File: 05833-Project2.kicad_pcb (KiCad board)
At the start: 2 copper layers, 13 parts, among them J1 BB, J2 FTDI, J3 AREF, J4 GPIO, U1 LM7805, U2 ATmega328-P, Y1 16MHz Resonator

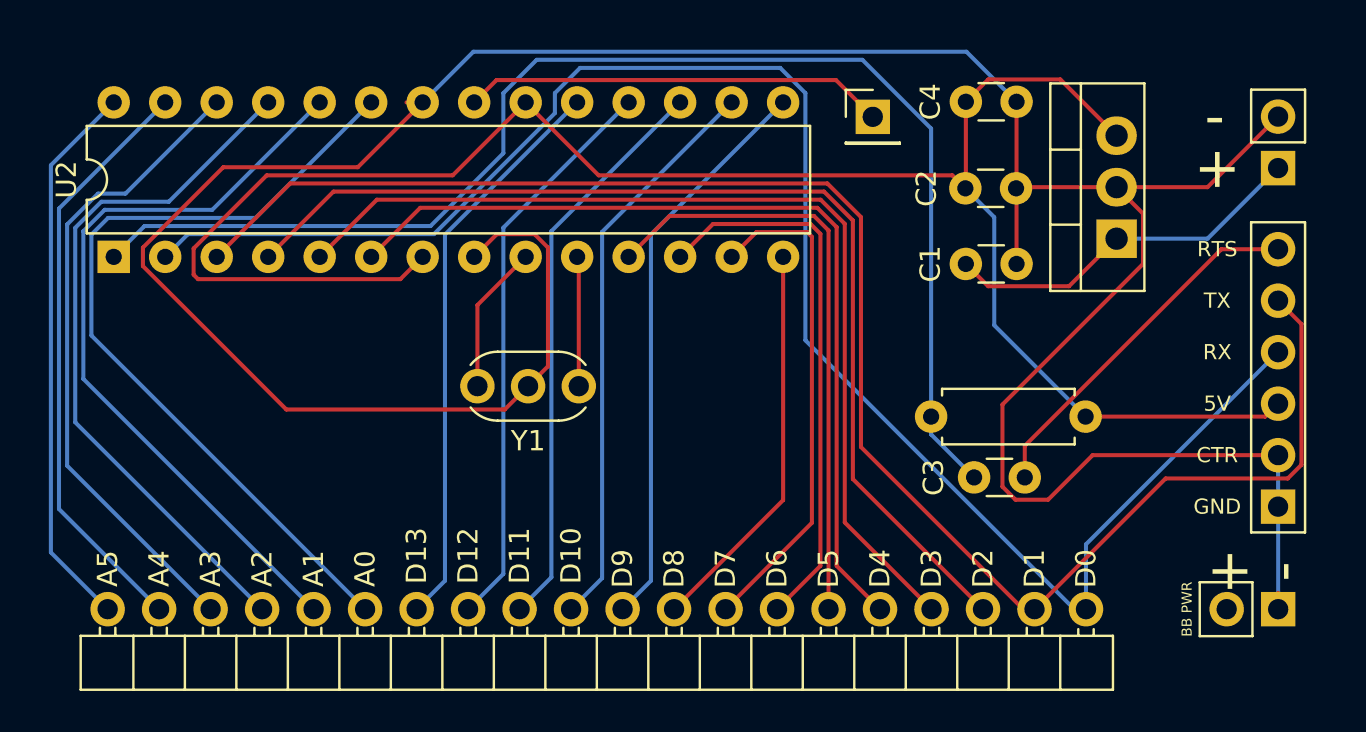
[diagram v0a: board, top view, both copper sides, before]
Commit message: Updates to the edge cuts
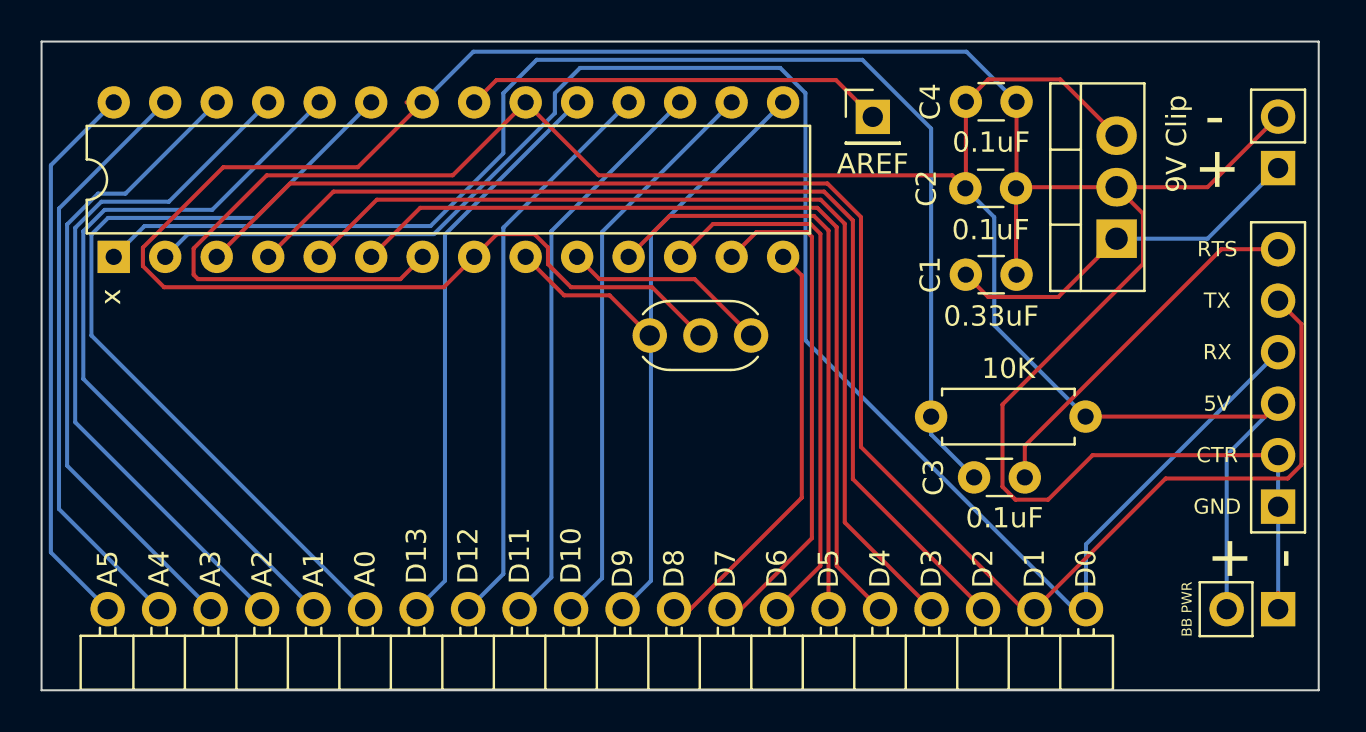
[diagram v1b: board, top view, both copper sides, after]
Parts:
- moved Y1 8.86 mm to (79.0, 64.0)
- moved C1 0.53 mm to (89.6, 61.0)
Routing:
- net +5V: track 93.4 -> 104.6 mm
- net Net-(U2-XTAL2/PB7): track 6.41 -> 10.2 mm
- net GND: track 148.0 -> 146.1 mm
- net /D8: track 19.6 -> 20.8 mm
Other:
- board outline added: 63 x 32 mm
- board text added: "x"
